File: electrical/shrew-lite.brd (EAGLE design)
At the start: 15.5 x 24 mm, 47 parts, among them IC1 Vreg +3V3, U1 ESP32-PICO-D4, U2 SX1280IMLTRT, U3 DRV8231DSGR, U4 DRV8231DSGR, X1 PIN-1X-BIG, X2 PIN-1X-BIG, X3 PIN-1X-BIG, X4 PIN-1X-BIG, X5 PIN-1X-MED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

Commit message: second gen gerbers
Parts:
- moved R4 0.30 mm to (11.2, 8.90)
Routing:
- net +24V: track 11.5 -> 12.2 mm
- net GND: vias 35 -> 34
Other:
- board text added: "A"
- board text added: "B"
- board text added: "SHREW LITE"
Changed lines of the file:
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@@
 <layer number="21" name="tPlace" color="7" fill="1" visible="yes" active="yes"/>
 <layer number="22" name="bPlace" color="7" fill="1" visible="yes" active="yes"/>
-<layer number="23" name="tOrigins" color="15" fill="1" visible="no" active="yes"/>
-<layer number="24" name="bOrigins" color="15" fill="1" visible="no" active="yes"/>
+<layer number="23" name="tOrigins" color="15" fill="1" visible="yes" active="yes"/>
+<layer number="24" name="bOrigins" color="15" fill="1" visible="yes" active="yes"/>
 <layer number="25" name="tNames" color="7" fill="1" visible="no" active="yes"/>
 <layer number="26" name="bNames" color="7" fill="1" visible="no" active="yes"/>
@@
 <layer number="28" name="bValues" color="7" fill="1" visible="no" active="yes"/>
 <layer number="29" name="tStop" color="7" fill="3" visible="no" active="yes"/>
-<layer number="30" name="bStop" color="7" fill="6" visible="no" active="yes"/>
+<layer number="30" name="bStop" color="7" fill="6" visible="yes" active="yes"/>
 <layer number="31" name="tCream" color="7" fill="4" visible="no" active="yes"/>
 <layer number="32" name="bCream" color="7" fill="5" visible="no" active="yes"/>
@@
 <wire x1="12.79" y1="4.13" x2="12.79" y2="3.74" width="0.254" layer="29"/>
 <rectangle x1="6" y1="3.5" x2="11.1" y2="4.3" layer="29"/>
-<rectangle x1="3" y1="3.3" x2="7.2" y2="4.8" layer="30"/>
+<rectangle x1="3" y1="3.7" x2="7.2" y2="4.8" layer="30"/>
 <wire x1="4.43" y1="3.93" x2="4.57" y2="3.93" width="0" layer="41"/>
 <wire x1="12.23" y1="3.93" x2="12.36" y2="3.93" width="0" layer="41"/>
@@
 <text x="0.3" y="8.5" size="1" layer="21" align="center-left">BAT+</text>
 <text x="15.3" y="8.5" size="1" layer="21" rot="R180" align="center-left">GND</text>
-<text x="13.3" y="6.3" size="1" layer="22" rot="MR0" align="center-left">GND</text>
+<text x="12.8" y="7.2" size="1" layer="22" rot="MR270" align="center-left">GND</text>
 <text x="2" y="7.4" size="1" layer="22" rot="MR180" align="center-left">BAT+</text>
 <text x="2.5" y="12" size="1" layer="22" rot="MR180" align="center-left">19</text>
@@
 <text x="2.6" y="16" size="0.8" layer="22" rot="MR180" align="center-left">3</text>
 <text x="2.6" y="18.4" size="0.8" layer="22" rot="MR180" align="center-left">1</text>
+<text x="9.9" y="11.7" size="0.9" layer="22" font="vector" ratio="10" rot="MR0" align="center-left">SHREW
+LITE</text>
+<text x="4.35" y="1.6" size="0.8" layer="21" font="vector" align="center">A</text>
+<text x="12.16" y="1.6" size="0.8" layer="21" font="vector" align="center">B</text>
+<text x="11.98" y="1.6" size="0.8" layer="22" font="vector" rot="MR0" align="center">B</text>
+<text x="4.17" y="1.6" size="0.8" layer="22" font="vector" rot="MR0" align="center">A</text>
 </plain>
 <attributes>
@@
 <attribute name="VALUE" x="5.5095" y="5.3705" size="0.4064" layer="28" rot="MR90"/>
 </element>
-<element name="R4" library="shrew-common" package="0402-RES" value="" x="11.2" y="8.6" smashed="yes" rot="MR180">
-<attribute name="NAME" x="10.311" y="7.9015" size="1.016" layer="26" font="vector" rot="MR180"/>
-<attribute name="VALUE" x="10.1205" y="9.743" size="0.4064" layer="28" rot="MR180"/>
+<element name="R4" library="shrew-common" package="0402-RES" value="" x="11.2" y="8.9" smashed="yes" rot="MR180">
+<attribute name="NAME" x="10.311" y="8.2015" size="1.016" layer="26" font="vector" rot="MR180"/>
+<attribute name="VALUE" x="10.1205" y="10.043" size="0.4064" layer="28" rot="MR180"/>
 </element>
 <element name="X7" library="shrew-core" package="PAD-1X-MED" value="PIN-1X-MED" x="1.16" y="6.8"/>
@@
 <via x="14.5" y="13.7" extent="1-16" drill="0.3" shape="octagon"/>
 <via x="9.1" y="14.7" extent="1-16" drill="0.3" shape="octagon"/>
-<via x="9.6" y="11.65" extent="1-16" drill="0.3" shape="octagon"/>
 <contactref element="C11" pad="2"/>
 <polygon width="0.1524" layer="1" spacing="0.1524" isolate="0.1524" thermals="no">
@@
 </polygon>
 <via x="12.81" y="5.4" extent="1-16" drill="0.3" shape="square"/>
+<wire x1="9.1" y1="14.7" x2="9.11" y2="14.69" width="0" layer="19" extent="1-15"/>
 </signal>
 <signal name="VDD_SDIO">
@@
 <contactref element="R4" pad="1"/>
 <wire x1="10.55" y1="10" x2="10.8" y2="10" width="0.4064" layer="16"/>
-<wire x1="10.55" y1="8.6" x2="10.55" y2="10" width="0.4064" layer="16"/>
+<wire x1="10.55" y1="8.9" x2="10.55" y2="10" width="0.4064" layer="16"/>
 <wire x1="10.55" y1="10" x2="10.5" y2="10" width="0.4064" layer="16"/>
 </signal>
@@
 <contactref element="X5" pad="1"/>
 <via x="6.04" y="4.38" extent="1-16" drill="0.3" shape="square"/>
-<via x="6.04" y="3.81" extent="1-16" drill="0.3" shape="square"/>
+<via x="6.04" y="3.81" extent="1-16" drill="0.3" shape="octagon"/>
 <contactref element="C16" pad="1"/>
 <contactref element="C19" pad="1"/>
@@
 <wire x1="2.2" y1="4.4" x2="2.2033" y2="4.3967" width="0.3048" layer="1"/>
 <wire x1="2.2033" y1="4.3967" x2="3.4998125" y2="4.3967" width="0.3048" layer="1"/>
-<via x="2.84" y="4.38" extent="1-16" drill="0.3" shape="square"/>
-<via x="2.84" y="3.78" extent="1-16" drill="0.3" shape="square"/>
+<via x="2.84" y="4.58" extent="1-16" drill="0.3" shape="square"/>
+<via x="2.84" y="3.98" extent="1-16" drill="0.3" shape="octagon"/>
 <contactref element="X7" pad="1"/>
 <wire x1="2" y1="8.8" x2="2" y2="7.64" width="0.4064" layer="16"/>
 <wire x1="2" y1="7.64" x2="1.16" y2="6.8" width="0.4064" layer="16"/>
 <wire x1="1.16" y1="6.8" x2="1.16" y2="5.06" width="0.4064" layer="16"/>
-<wire x1="10.6" y1="7.3" x2="11.85" y2="8.55" width="0.1524" layer="16"/>
-<wire x1="11.85" y1="8.55" x2="11.85" y2="8.6" width="0.1524" layer="16"/>
 <polygon width="0.3048" layer="15" spacing="0.1524" isolate="0.3048" thermals="no">
 <vertex x="2.6" y="4.6"/>
@@
 <vertex x="2.6" y="3.6"/>
 </polygon>
+<wire x1="10.6" y1="7.3" x2="11.1" y2="7.8" width="0.1524" layer="16"/>
+<wire x1="11.1" y1="7.8" x2="11.4" y2="7.8" width="0.1524" layer="16"/>
+<wire x1="11.4" y1="7.8" x2="11.6" y2="8" width="0.1524" layer="16"/>
+<wire x1="11.6" y1="8" x2="11.6" y2="8.9" width="0.1524" layer="16"/>
+<wire x1="11.6" y1="8.9" x2="11.85" y2="8.9" width="0.1524" layer="16"/>
 </signal>
 <signal name="MOTOR3">
@@
 </board>
 </drawing>
+<compatibility>
+<note version="6.3" minversion="6.2.2" severity="warning">
+Since Version 6.2.2 text objects can contain more than one line,
+which will not be processed correctly with this version.
+</note>
+</compatibility>
 </eagle>

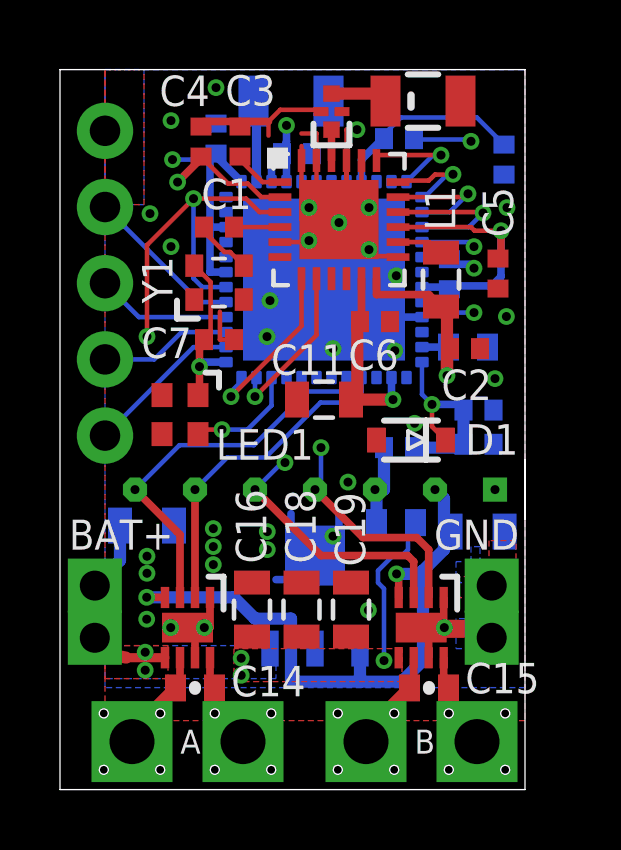
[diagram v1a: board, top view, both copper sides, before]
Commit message: placed a PCBA order for shrew-lite
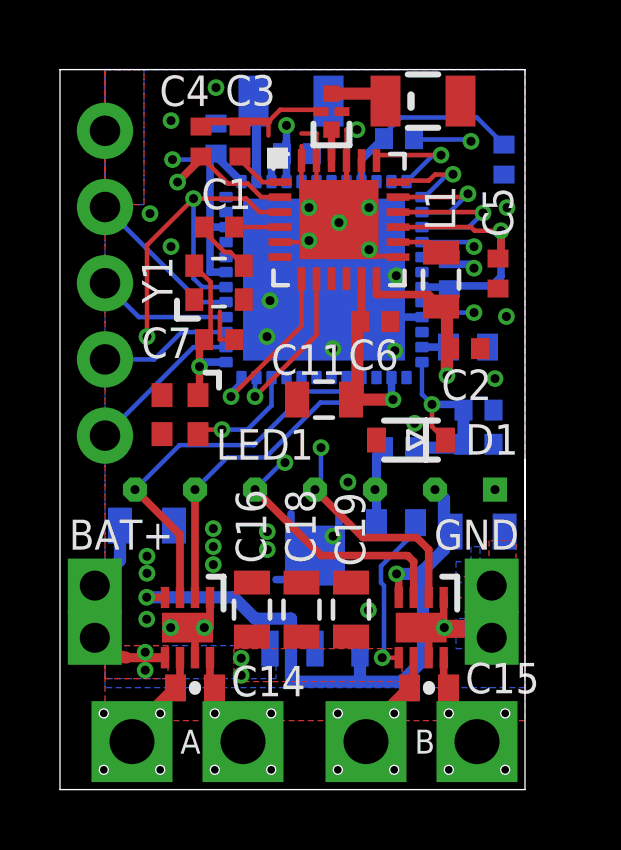
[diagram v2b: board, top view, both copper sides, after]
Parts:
- C11: value 10uF 25V -> 10u
- C14, C15: value (none) -> 100n
- C16, C18, C19, C20, C21: value (none) -> 10u
- R4: value (none) -> 68K
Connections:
- net V-ADC renamed N$4
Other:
- board text added: "V+"
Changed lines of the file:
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@@
 <layer number="28" name="bValues" color="7" fill="1" visible="no" active="yes"/>
 <layer number="29" name="tStop" color="7" fill="3" visible="no" active="yes"/>
-<layer number="30" name="bStop" color="7" fill="6" visible="yes" active="yes"/>
+<layer number="30" name="bStop" color="7" fill="6" visible="no" active="yes"/>
 <layer number="31" name="tCream" color="7" fill="4" visible="no" active="yes"/>
 <layer number="32" name="bCream" color="7" fill="5" visible="no" active="yes"/>
@@
 <text x="15.3" y="8.5" size="1" layer="21" rot="R180" align="center-left">GND</text>
 <text x="12.8" y="7.2" size="1" layer="22" rot="MR270" align="center-left">GND</text>
-<text x="2" y="7.4" size="1" layer="22" rot="MR180" align="center-left">BAT+</text>
+<text x="0.83" y="7.99" size="1" layer="22" rot="MR90" align="center-left">V+</text>
 <text x="2.5" y="12" size="1" layer="22" rot="MR180" align="center-left">19</text>
 <text x="2.5" y="14.6" size="1" layer="22" rot="MR180" align="center-left">22</text>
@@
 <attribute name="VALUE" x="4.675" y="10.53" size="1.27" layer="27" rot="R90"/>
 </element>
-<element name="C11" library="shrew-common" package="0805" value="10uF 25V" x="8.8" y="13" smashed="yes" rot="R180">
+<element name="C11" library="shrew-common" package="0805" value="10u" x="8.8" y="13" smashed="yes" rot="R180">
 <attribute name="NAME" x="7.038" y="13.8255" size="1.016" layer="25" font="vector"/>
 </element>
@@
 <element name="X3" library="shrew-core" package="PAD-1X-BIG" value="PIN-1X-BIG" x="10.2" y="1.6" smashed="yes"/>
 <element name="X4" library="shrew-core" package="PAD-1X-BIG" value="PIN-1X-BIG" x="13.9" y="1.6" smashed="yes"/>
-<element name="C14" library="shrew-common" package="0402-CAP" value="" x="4.5" y="3.39" smashed="yes" rot="R180">
+<element name="C14" library="shrew-common" package="0402-CAP" value="100n" x="4.5" y="3.39" smashed="yes" rot="R180">
 <attribute name="NAME" x="5.711" y="3.1085" size="1.016" layer="25" font="vector"/>
 <attribute name="VALUE" x="5.5795" y="4.533" size="0.4064" layer="27" rot="R180"/>
 </element>
-<element name="C15" library="shrew-common" package="0402-CAP" value="" x="12.3" y="3.39" smashed="yes" rot="R180">
+<element name="C15" library="shrew-common" package="0402-CAP" value="100n" x="12.3" y="3.39" smashed="yes" rot="R180">
 <attribute name="NAME" x="13.511" y="3.2085" size="1.016" layer="25" font="vector"/>
 <attribute name="VALUE" x="13.3795" y="4.533" size="0.4064" layer="27" rot="R180"/>
@@
 <element name="X5" library="shrew-core" package="PAD-1X-MED" value="PIN-1X-MED" x="1.16" y="5.06" smashed="yes"/>
 <element name="X6" library="shrew-core" package="PAD-1X-MED" value="PIN-1X-MED" x="14.39" y="5.06" smashed="yes"/>
-<element name="C16" library="shrew-common" package="0805" value="" x="6.4" y="6" smashed="yes" rot="R90">
+<element name="C16" library="shrew-common" package="0805" value="10u" x="6.4" y="6" smashed="yes" rot="R90">
 <attribute name="NAME" x="6.8745" y="7.538" size="1.016" layer="25" font="vector" rot="R90"/>
 <attribute name="VALUE" x="7.797" y="4.984" size="0.4064" layer="27" rot="R90"/>
 </element>
-<element name="C18" library="shrew-common" package="0805" value="" x="8.05" y="6" smashed="yes" rot="R90">
+<element name="C18" library="shrew-common" package="0805" value="10u" x="8.05" y="6" smashed="yes" rot="R90">
 <attribute name="NAME" x="8.5245" y="7.538" size="1.016" layer="25" font="vector" rot="R90"/>
 <attribute name="VALUE" x="9.447" y="4.984" size="0.4064" layer="27" rot="R90"/>
 </element>
-<element name="C19" library="shrew-common" package="0805" value="" x="9.7" y="6" smashed="yes" rot="R90">
+<element name="C19" library="shrew-common" package="0805" value="10u" x="9.7" y="6" smashed="yes" rot="R90">
 <attribute name="NAME" x="10.1745" y="7.438" size="1.016" layer="25" font="vector" rot="R90"/>
 <attribute name="VALUE" x="11.097" y="4.984" size="0.4064" layer="27" rot="R90"/>
 </element>
-<element name="C20" library="shrew-common" package="0805" value="" x="2.9" y="8.8" smashed="yes" rot="MR180">
+<element name="C20" library="shrew-common" package="0805" value="10u" x="2.9" y="8.8" smashed="yes" rot="MR180">
 <attribute name="NAME" x="2.138" y="7.9745" size="1.016" layer="26" font="vector" rot="MR180"/>
 <attribute name="VALUE" x="1.884" y="10.197" size="0.4064" layer="28" rot="MR180"/>
 </element>
-<element name="C21" library="shrew-common" package="0805" value="" x="13.92" y="8.6" smashed="yes" rot="MR180">
+<element name="C21" library="shrew-common" package="0805" value="10u" x="13.92" y="8.6" smashed="yes" rot="MR180">
 <attribute name="NAME" x="12.558" y="7.6745" size="1.016" layer="26" font="vector" rot="MR180"/>
 <attribute name="VALUE" x="12.904" y="9.997" size="0.4064" layer="28" rot="MR180"/>
@@
 <attribute name="VALUE" x="5.5095" y="5.3705" size="0.4064" layer="28" rot="MR90"/>
 </element>
-<element name="R4" library="shrew-common" package="0402-RES" value="" x="11.2" y="8.9" smashed="yes" rot="MR180">
+<element name="R4" library="shrew-common" package="0402-RES" value="68K" x="11.2" y="8.9" smashed="yes" rot="MR180">
 <attribute name="NAME" x="10.311" y="8.2015" size="1.016" layer="26" font="vector" rot="MR180"/>
 <attribute name="VALUE" x="10.1205" y="10.043" size="0.4064" layer="28" rot="MR180"/>
@@
 <wire x1="3.9" y1="8.6" x2="2.5" y2="10" width="0.254" layer="1"/>
 </signal>
-<signal name="V-ADC">
-<contactref element="R3" pad="2"/>
-<wire x1="10.8" y1="10" x2="10.8" y2="11.4" width="0.4064" layer="16"/>
-<contactref element="JP1" pad="3"/>
-<contactref element="R4" pad="1"/>
-<wire x1="10.55" y1="10" x2="10.8" y2="10" width="0.4064" layer="16"/>
-<wire x1="10.55" y1="8.9" x2="10.55" y2="10" width="0.4064" layer="16"/>
-<wire x1="10.55" y1="10" x2="10.5" y2="10" width="0.4064" layer="16"/>
-</signal>
 <signal name="N$5">
 <contactref element="U1" pad="17"/>
@@
 </polygon>
 <contactref element="IC1" pad="3"/>
-<contactref element="R4" pad="2"/>
-<via x="10.8" y="4.3" extent="1-16" drill="0.3" shape="octagon"/>
-<wire x1="10.8" y1="4.3" x2="10.8" y2="6.7" width="0.1524" layer="16"/>
-<wire x1="10.8" y1="6.7" x2="10.6" y2="6.9" width="0.1524" layer="16"/>
-<wire x1="10.6" y1="6.9" x2="10.6" y2="7.3" width="0.1524" layer="16"/>
 <wire x1="1.16" y1="5.06" x2="1.9" y2="4.46" width="0.4064" layer="1"/>
 <wire x1="1.9" y1="4.46" x2="2.2" y2="4.4" width="0.4064" layer="1"/>
@@
 <vertex x="2.6" y="3.6"/>
 </polygon>
-<wire x1="10.6" y1="7.3" x2="11.1" y2="7.8" width="0.1524" layer="16"/>
-<wire x1="11.1" y1="7.8" x2="11.4" y2="7.8" width="0.1524" layer="16"/>
-<wire x1="11.4" y1="7.8" x2="11.6" y2="8" width="0.1524" layer="16"/>
-<wire x1="11.6" y1="8" x2="11.6" y2="8.9" width="0.1524" layer="16"/>
-<wire x1="11.6" y1="8.9" x2="11.85" y2="8.9" width="0.1524" layer="16"/>
+<contactref element="R4" pad="2"/>
+<wire x1="11.85" y1="8.9" x2="11.57" y2="8.62" width="0.1524" layer="16"/>
+<wire x1="11.57" y1="8.62" x2="11.57" y2="8.32" width="0.1524" layer="16"/>
+<wire x1="11.57" y1="8.32" x2="10.7" y2="7.45" width="0.1524" layer="16"/>
+<wire x1="10.7" y1="7.45" x2="10.7" y2="6.9" width="0.1524" layer="16"/>
+<wire x1="10.7" y1="6.9" x2="10.8" y2="6.8" width="0.1524" layer="16"/>
+<wire x1="10.74" y1="4.3967" x2="11.2898125" y2="4.3967" width="0.1524" layer="1"/>
+<via x="10.74" y="4.3967" extent="1-16" drill="0.3" shape="octagon"/>
+<wire x1="10.8" y1="6.8" x2="10.8" y2="4.3967" width="0.1524" layer="16"/>
+<wire x1="10.8" y1="4.3967" x2="10.74" y2="4.3967" width="0.1524" layer="16"/>
 </signal>
 <signal name="MOTOR3">
@@
 <wire x1="12.95" y1="1.6" x2="13.9" y2="1.6" width="0.254" layer="1"/>
 </signal>
+<signal name="N$4">
+<contactref element="R3" pad="2"/>
+<contactref element="R4" pad="1"/>
+<contactref element="JP1" pad="3"/>
+<wire x1="10.55" y1="8.9" x2="10.55" y2="10" width="0.3048" layer="16"/>
+<wire x1="10.55" y1="10" x2="10.55" y2="11.15" width="0.3048" layer="16"/>
+<wire x1="10.55" y1="11.15" x2="10.8" y2="11.4" width="0.3048" layer="16"/>
+<wire x1="10.5" y1="10" x2="10.55" y2="10" width="0.3048" layer="16"/>
+</signal>
 </signals>

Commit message: wip
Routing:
- net GND: track 53.4 -> 50.2 mm
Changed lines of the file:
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@@
 <layers>
 <layer number="1" name="Top" color="4" fill="1" visible="yes" active="yes"/>
-<layer number="2" name="Route2" color="1" fill="3" visible="no" active="yes"/>
+<layer number="2" name="Route2" color="1" fill="3" visible="yes" active="yes"/>
 <layer number="3" name="Route3" color="4" fill="3" visible="no" active="no"/>
 <layer number="4" name="Route4" color="1" fill="4" visible="no" active="no"/>
@@
 <layer number="13" name="Route13" color="4" fill="5" visible="no" active="no"/>
 <layer number="14" name="Route14" color="1" fill="6" visible="no" active="no"/>
-<layer number="15" name="Route15" color="4" fill="6" visible="no" active="yes"/>
+<layer number="15" name="Route15" color="4" fill="6" visible="yes" active="yes"/>
 <layer number="16" name="Bottom" color="1" fill="1" visible="yes" active="yes"/>
 <layer number="17" name="Pads" color="2" fill="1" visible="yes" active="yes"/>
@@
 <wire x1="11.16" y1="14.62" x2="11.82" y2="13.96" width="0.1524" layer="15"/>
 <wire x1="11.82" y1="13.96" x2="11.82" y2="12.21" width="0.1524" layer="15"/>
-<wire x1="9.6" y1="11.65" x2="9.6" y2="14.2" width="0.1524" layer="15"/>
-<wire x1="9.6" y1="14.2" x2="9.11" y2="14.69" width="0.1524" layer="15"/>
 <via x="3" y="19.2" extent="1-16" drill="0.3" shape="octagon"/>
 <contactref element="U4" pad="9"/>
@@
 </polygon>
 <via x="12.81" y="5.4" extent="1-16" drill="0.3" shape="square"/>
-<wire x1="9.1" y1="14.7" x2="9.11" y2="14.69" width="0" layer="19" extent="1-15"/>
 </signal>
 <signal name="VDD_SDIO">
